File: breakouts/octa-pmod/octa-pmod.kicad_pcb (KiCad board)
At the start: 2 copper layers, 54.5 x 46.4 mm, 19 parts, among them J1 PMOD, J10 PMOD, J12 PWR, J14 PWR, J15 PMOD, J16 PMOD, J2 PMOD, J3 S7 Mini, J4 S7 Mini, J5 PWR, J6 PWR, J7 PMOD, J8 PMOD, J9 PMOD, M1 M3, M2 M3, M3 M3, M4 M3

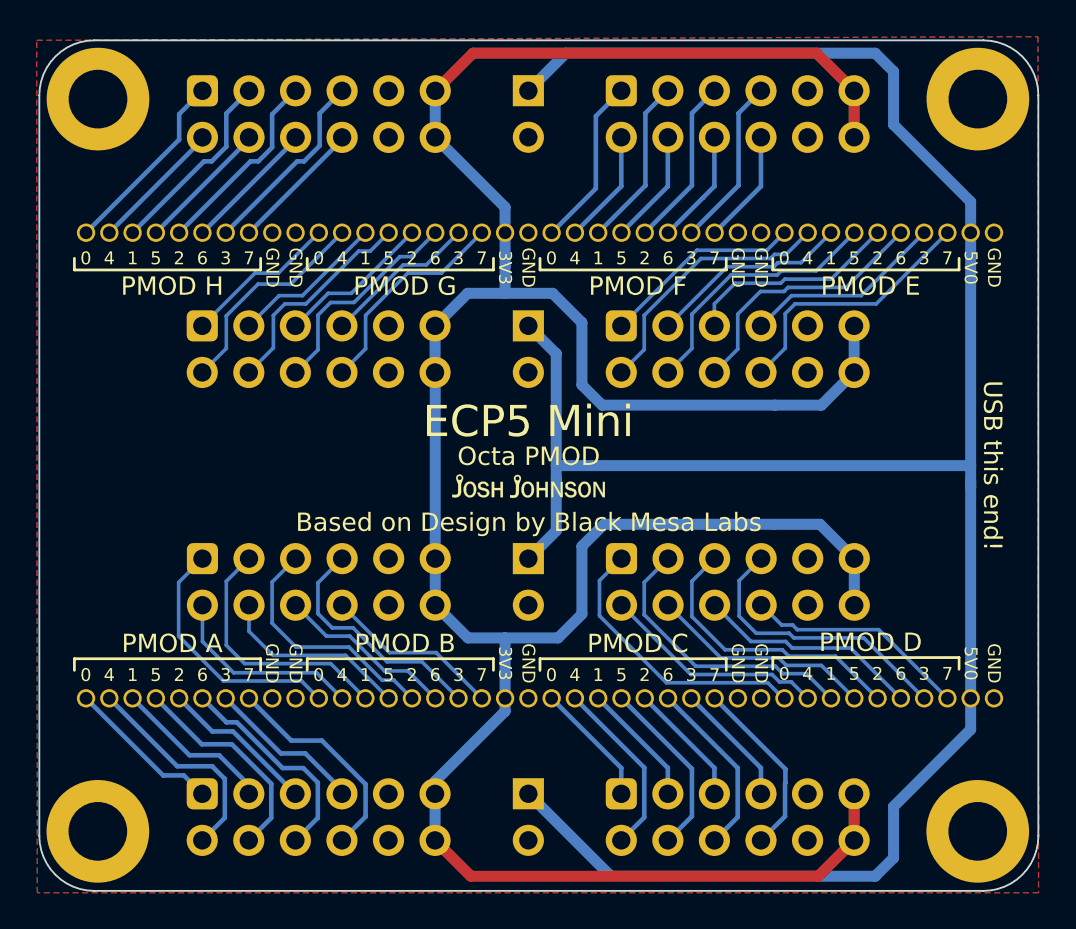
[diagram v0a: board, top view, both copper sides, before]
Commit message: update silk to clear connectors
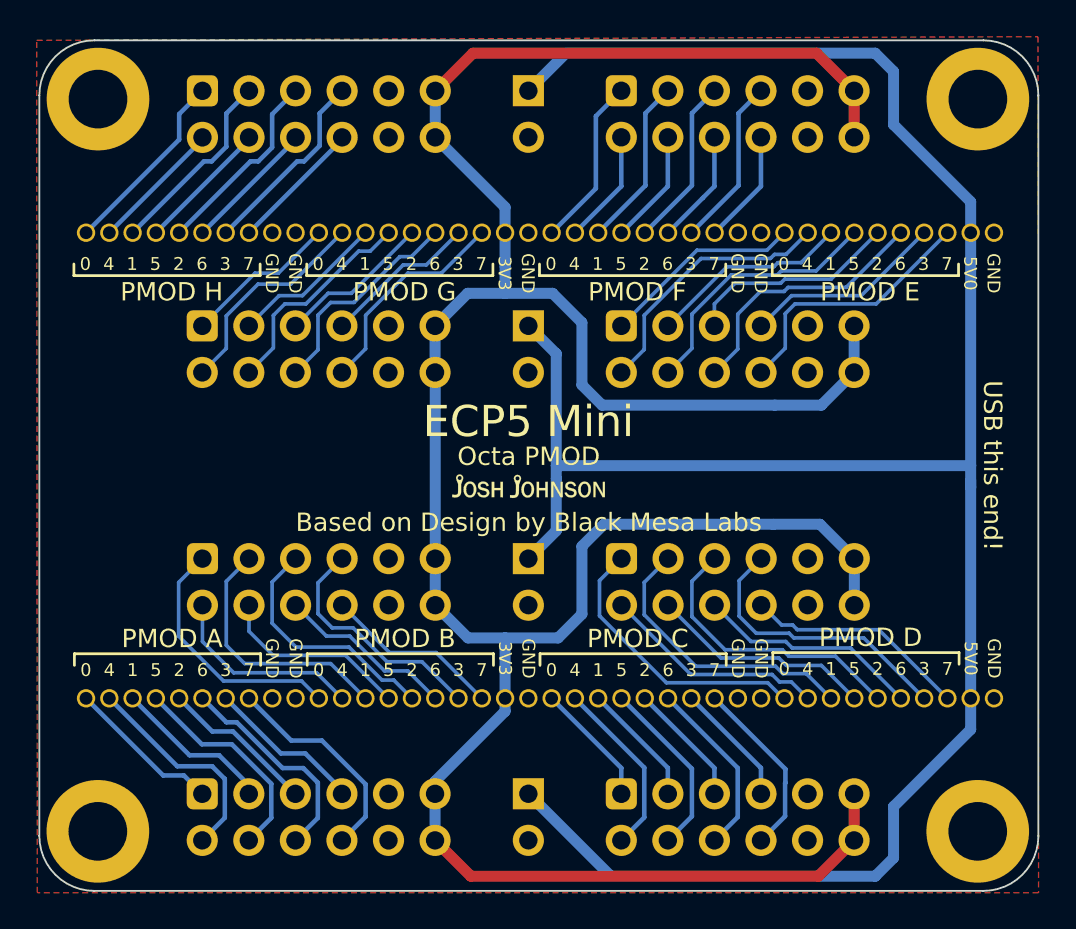
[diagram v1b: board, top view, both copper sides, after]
